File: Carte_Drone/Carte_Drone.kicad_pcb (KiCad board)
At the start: 2 copper layers, 1 part

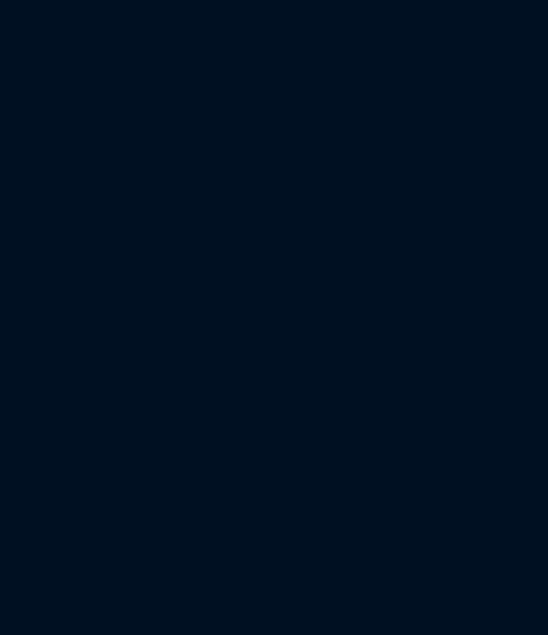
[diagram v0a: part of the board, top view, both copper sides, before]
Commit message: Ajout et modifications d'empreintes
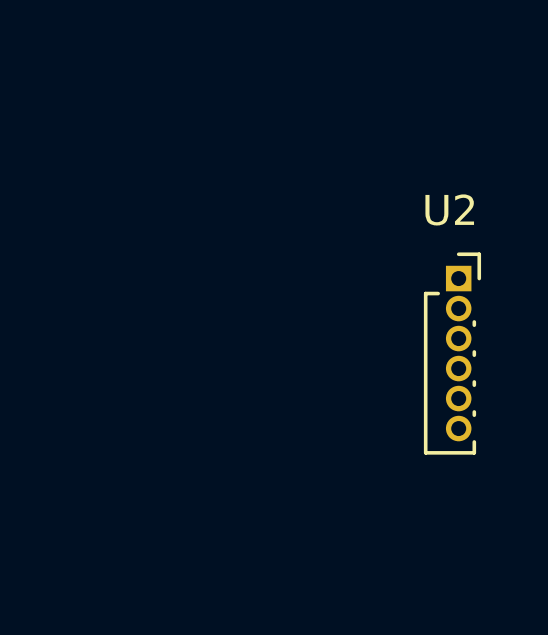
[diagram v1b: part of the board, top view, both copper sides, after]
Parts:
- added U2: ~, Connector_PinSocket_1.00mm:PinSocket_1x06_P1.00mm_Vertical, F.Cu at (195.0, 63.0)

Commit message: Ajout et modifications d'empreintes 2
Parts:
- added U3: ~, Connector_PinSocket_1.27mm:PinSocket_1x03_P1.27mm_Vertical, F.Cu at (186.0, 50.5)
- U2: footprint Connector_PinSocket_1.00mm:PinSocket_1x06_P1.00mm_Vertical -> Connector_PinSocket_1.27mm:PinSocket_1x06_P1.27mm_Vertical
- moved U2 2.17 mm to (193.0, 62.1)

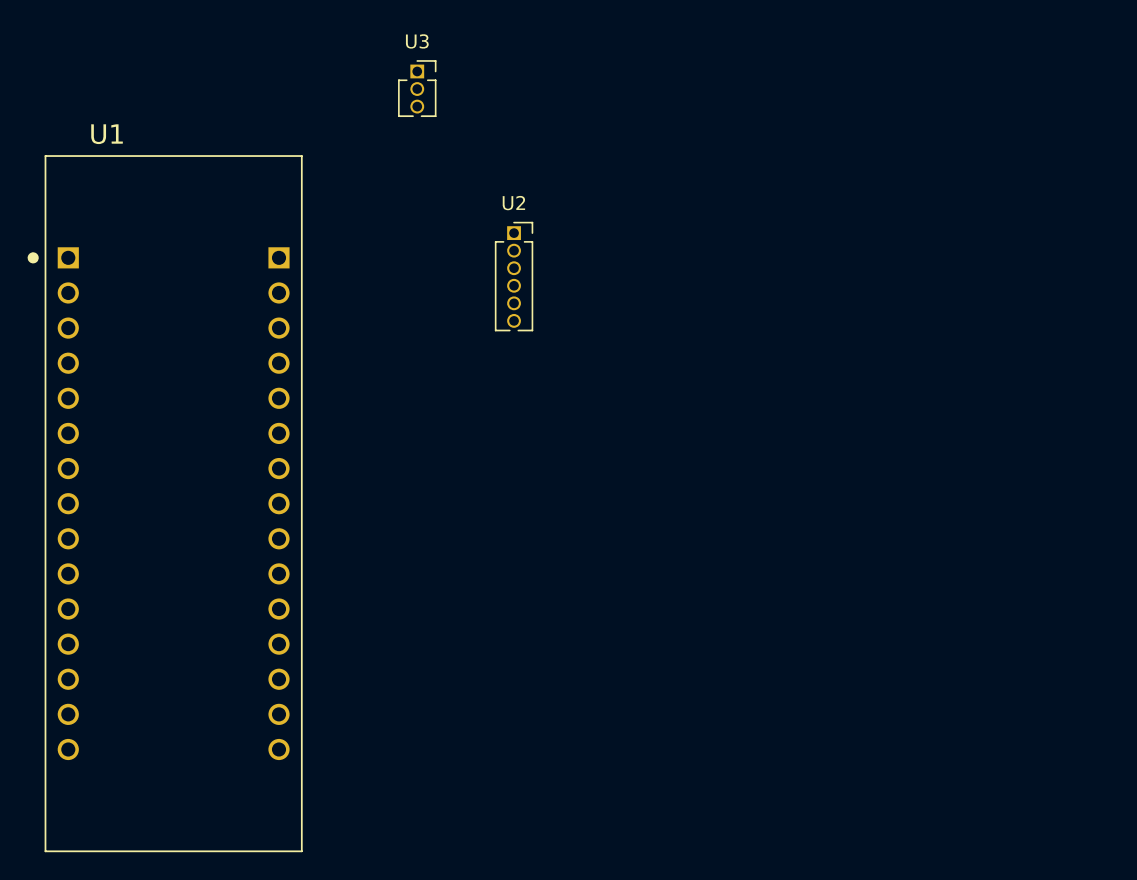
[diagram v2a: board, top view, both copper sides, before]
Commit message: Ajout connexion capteur son et microcontrôleur
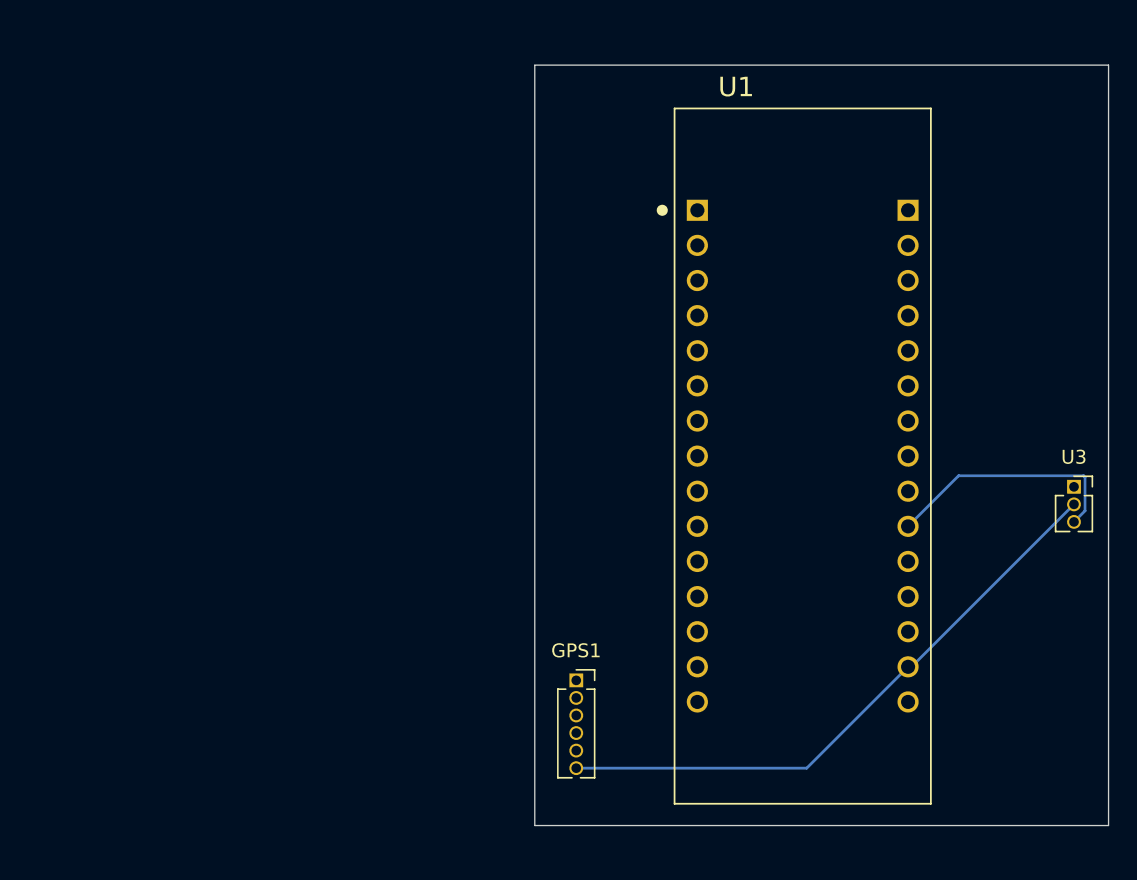
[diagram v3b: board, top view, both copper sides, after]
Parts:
- moved U3 56.2 mm to (233.5, 80.5)
- moved U1 45.6 mm to (213.9, 78.3)
- moved GPS1 32.7 mm to (197.5, 94.5)
- renumbered U2 to GPS1
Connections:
- U1 pad 10: unconnected-(U1-A2-Pad10) -> /Output
- U3 pad 3: unconnected-(U3-Output-Pad3) -> /Output
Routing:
- net /3V3: track 0.00 -> 43.9 mm
- net /Output: track 0.00 -> 17.9 mm
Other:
- board outline added: 41.5 x 55 mm

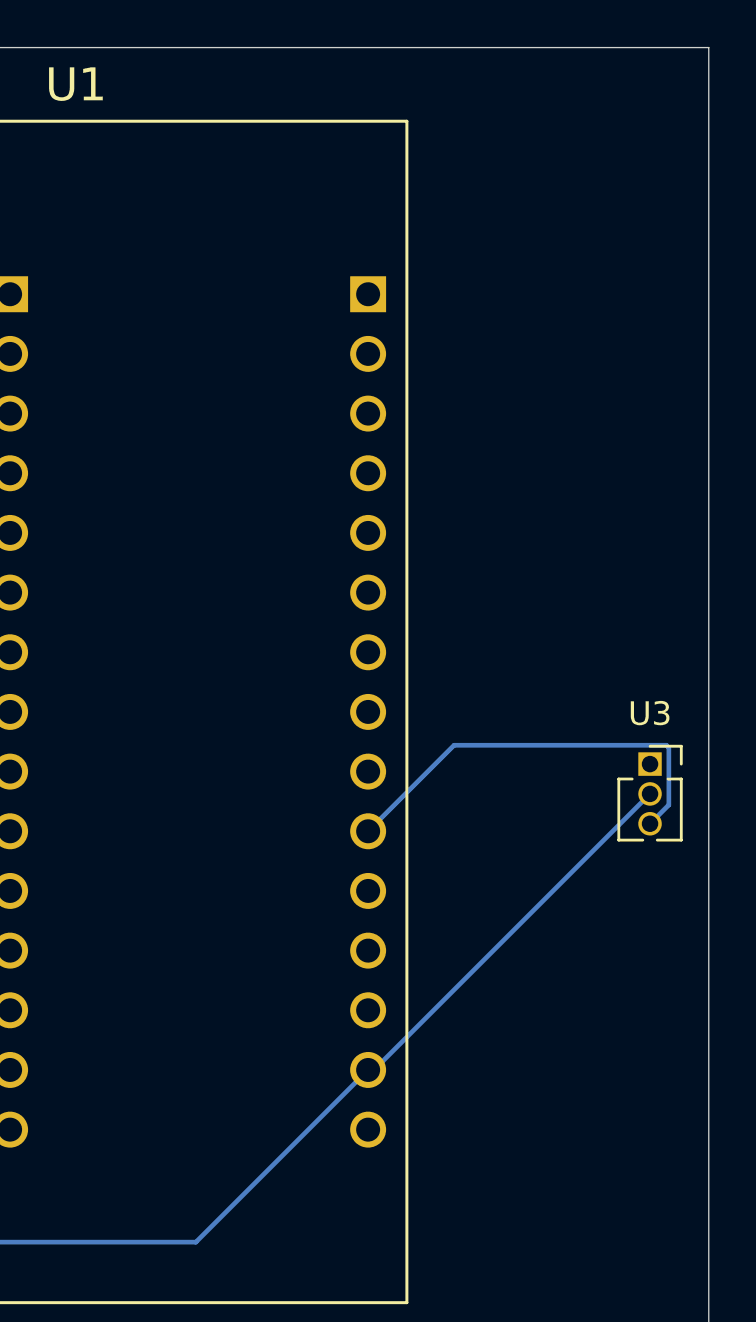
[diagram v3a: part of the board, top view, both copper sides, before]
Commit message: Ajout d'un composant et de documents
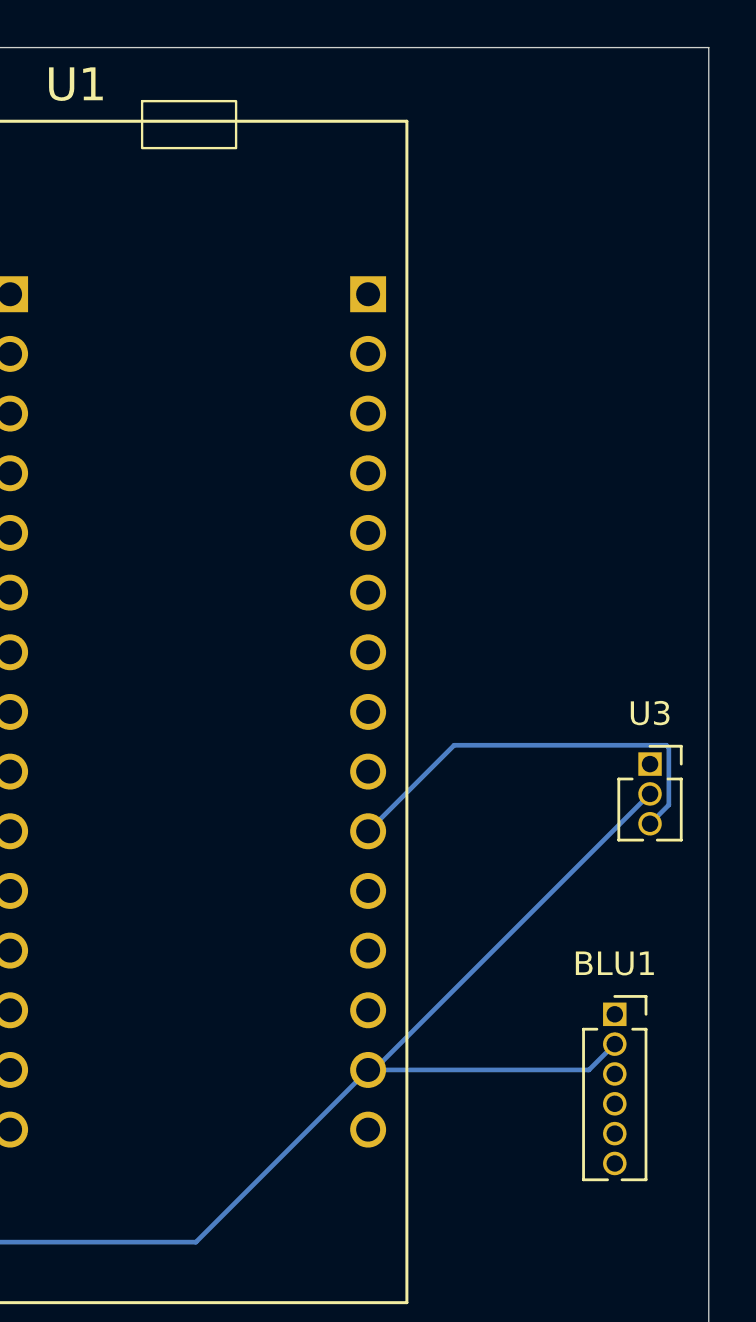
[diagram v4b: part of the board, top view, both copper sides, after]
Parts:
- added BLU1: ~, Connector_PinSocket_1.27mm:PinSocket_1x06_P1.27mm_Vertical, F.Cu at (232.0, 91.2)
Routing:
- net /3V3: track 43.9 -> 54.9 mm

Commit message: Fin de la création de la carte
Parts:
- moved BLU1 34.5 mm to (197.5, 92.5)
- moved GPS1 22.5 mm to (197.5, 72.0)
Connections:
- BLU1 pad 4: unconnected-(BLU1-TXD-Pad4) -> /TXB
- BLU1 pad 5: unconnected-(BLU1-RXD-Pad5) -> /RXB
- GPS1 pad 2: unconnected-(GPS1-RXD-Pad2) -> /RXG
- GPS1 pad 3: unconnected-(GPS1-TXD-Pad3) -> /TXG
- U1 pad 23: unconnected-(U1-D5-Pad23) -> /RXB
- U1 pad 24: unconnected-(U1-D4-Pad24) -> /TXB
- U1 pad 29: unconnected-(U1-D0/RX-Pad29) -> /TXG
- U1 pad 30: unconnected-(U1-D1/TX-Pad30) -> /RXG
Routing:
- net Earth: track 0.00 -> 31.2 mm
- net /TXB: track 0.00 -> 24.2 mm
- net /RXB: track 0.00 -> 22.9 mm
- net /3V3: track 54.9 -> 72.2 mm
- net /RXG: track 0.00 -> 16.6 mm
- net /TXG: track 0.00 -> 15.1 mm
- net /Output: track 17.9 -> 12.1 mm
- added copper zone on B.Cu, net Earth
